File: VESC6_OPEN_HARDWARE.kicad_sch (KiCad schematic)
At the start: 22 parts, among them P1 USB_OTG, P2 CAN2, P3 SWD, P4 HALL/Encoder, P5 CAN1, P6 ADC_SWITCH

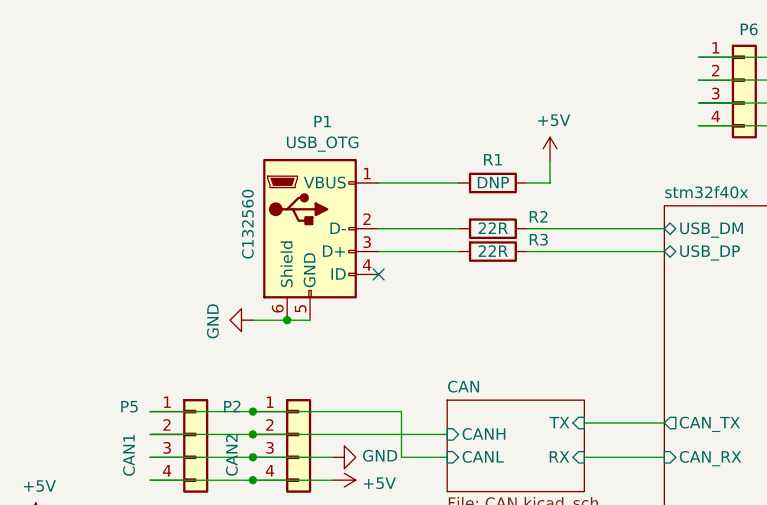
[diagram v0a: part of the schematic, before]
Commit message: added a USB-C connector and bumped the KiCAD version to 10
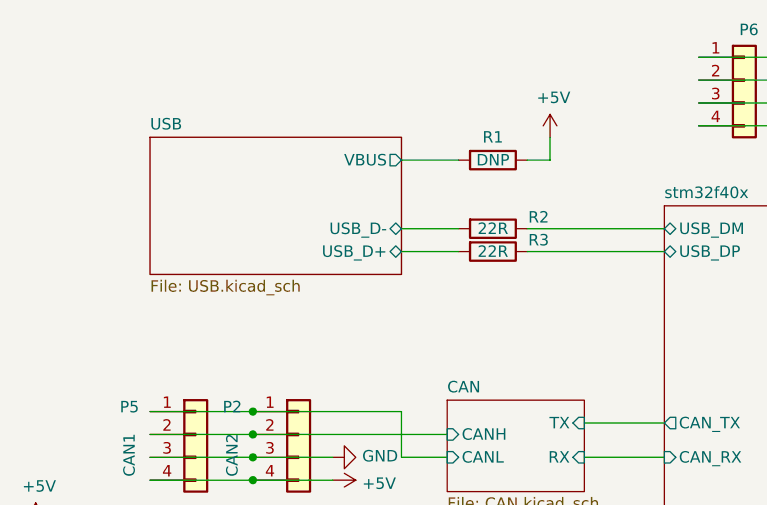
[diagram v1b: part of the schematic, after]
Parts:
- removed P1: USB_OTG, Connector_USB:USB_Micro-B_Molex_47346-0001, symbol bldc:USB_OTG
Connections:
- net USB/USB_D-: now reaches R2.2
- net USB/USB_D+: now reaches R3.2
- net USB/VBUS: now reaches R1.2
- no-connect marks 1 -> 0
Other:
- added sheet USB (USB.kicad_sch)
- moved on the sheet: R1

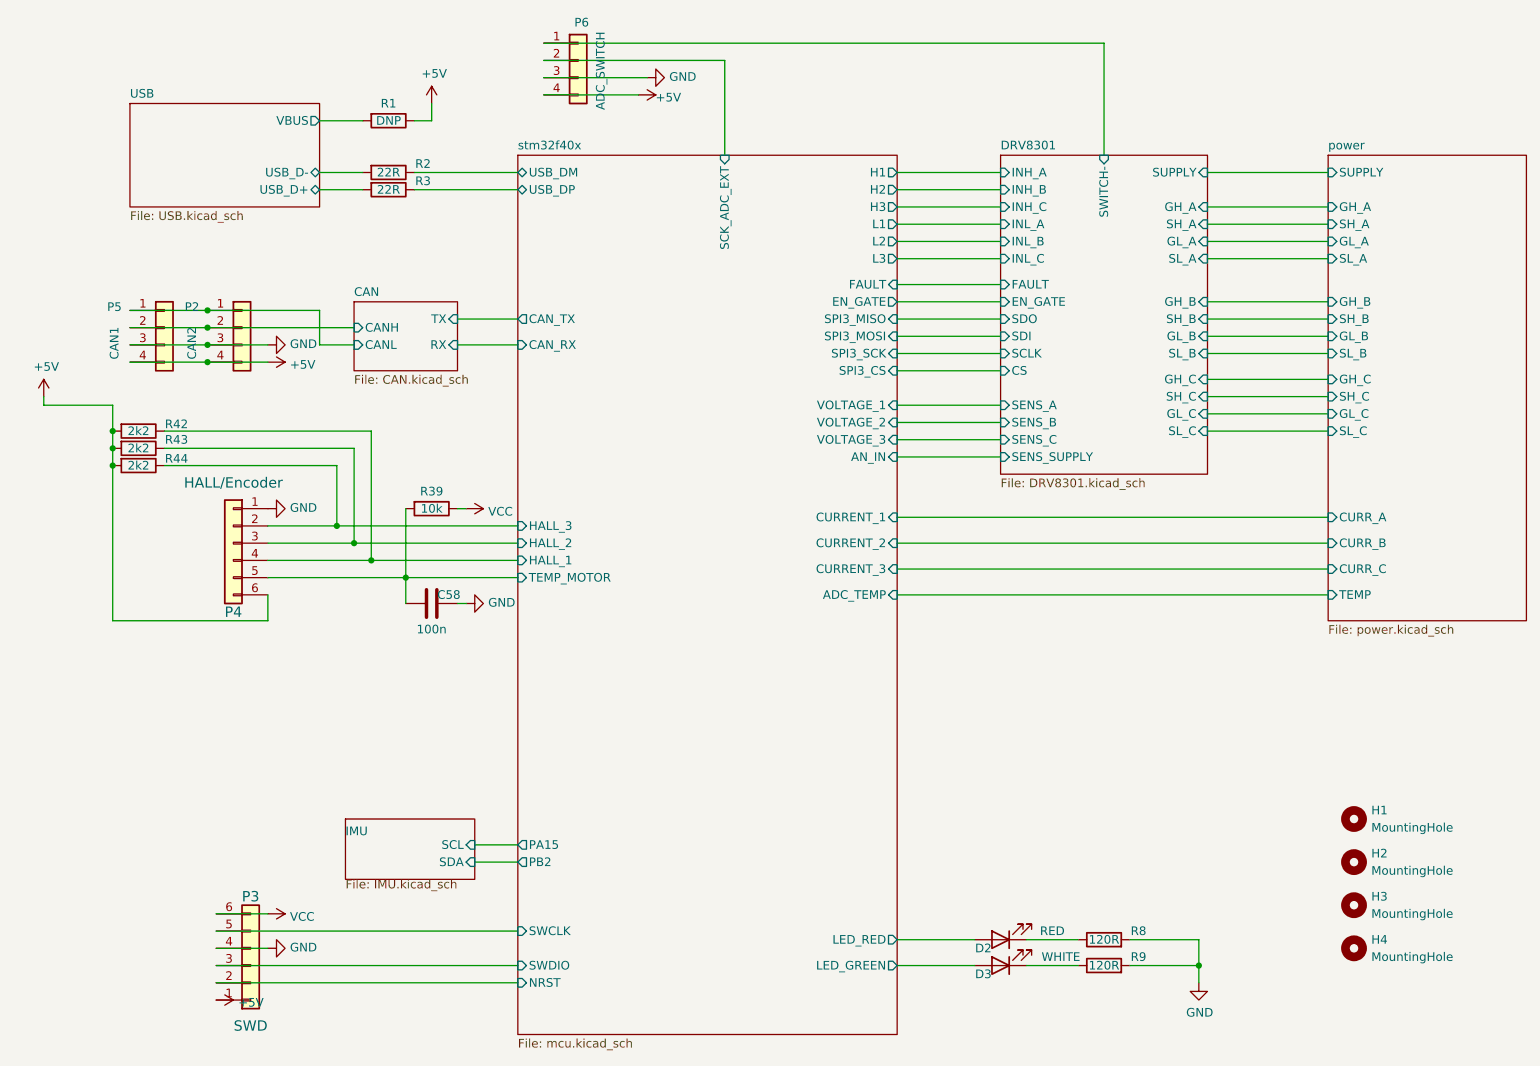
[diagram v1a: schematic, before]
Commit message: prep for chaneling. fixed the connector references, added cha to this schematic.
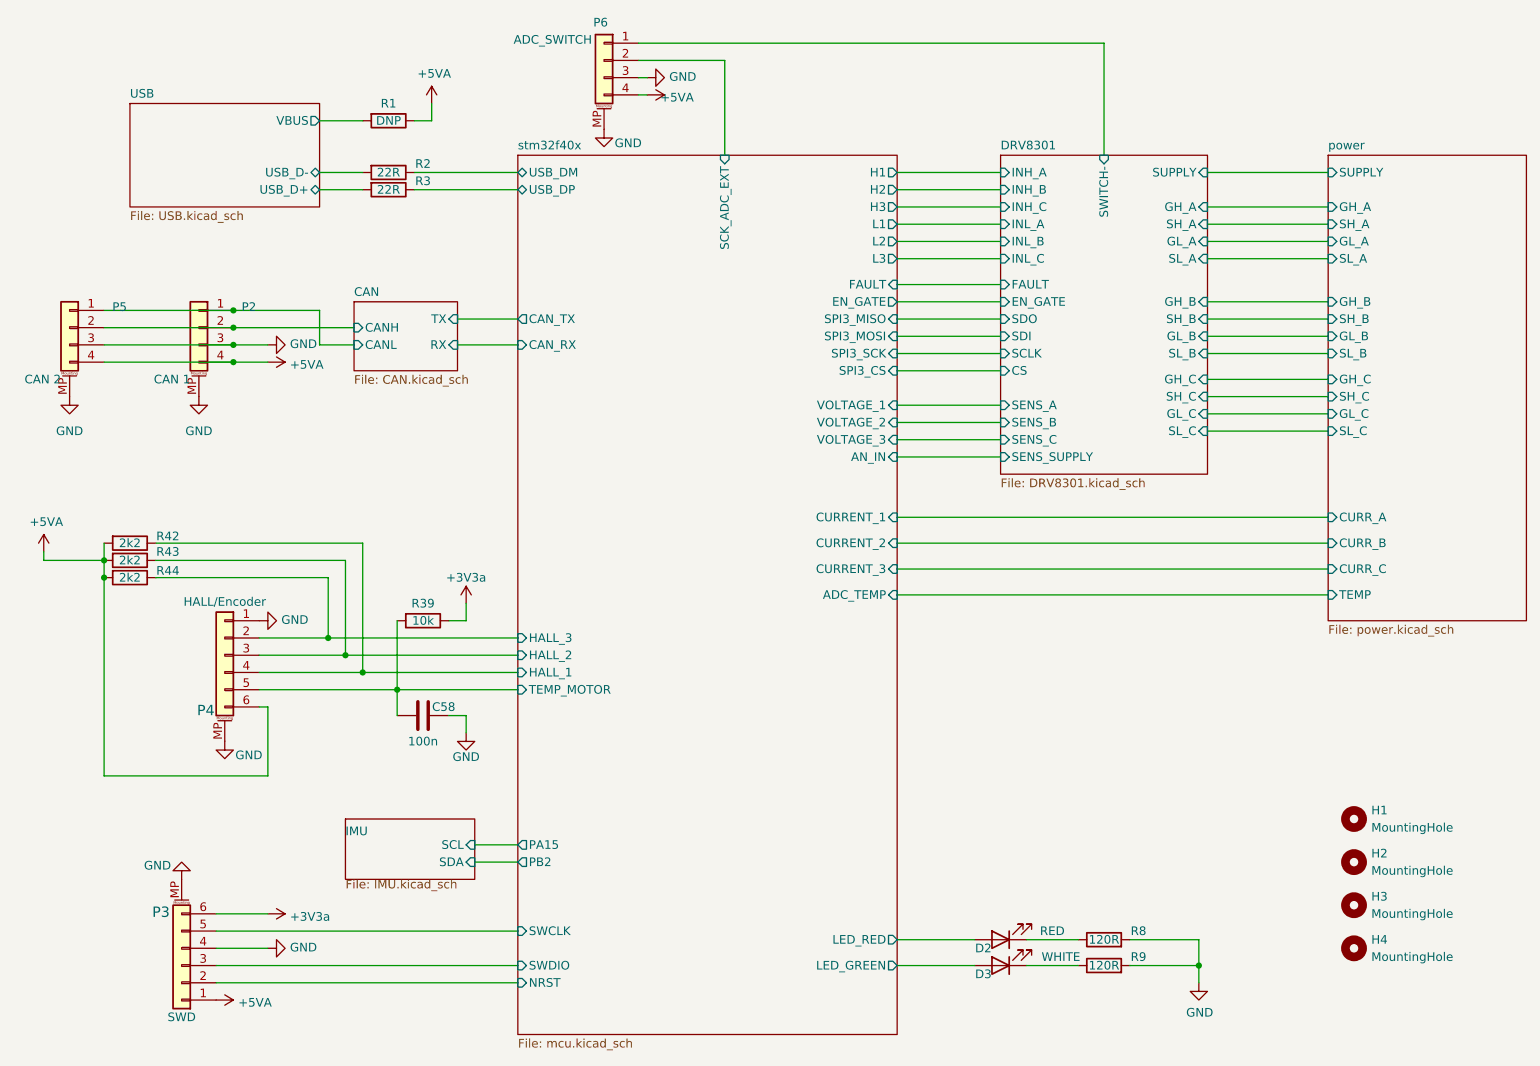
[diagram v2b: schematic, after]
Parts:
- P2: value CAN2 -> CAN 1; symbol Connector_Generic:Conn_01x04 -> Connector_Generic_MountingPin:Conn_01x04_MountingPin; Function (none) -> CAN 1
- P3: symbol Connector_Generic:Conn_01x06 -> Connector_Generic_MountingPin:Conn_01x06_MountingPin; Function (none) -> SWD
- P4: symbol Connector_Generic:Conn_01x06 -> Connector_Generic_MountingPin:Conn_01x06_MountingPin; Function (none) -> SENSE
- P5: value CAN1 -> CAN 2; symbol Connector_Generic:Conn_01x04 -> Connector_Generic_MountingPin:Conn_01x04_MountingPin; Function (none) -> CAN 2
- P6: symbol Connector_Generic:Conn_01x04 -> Connector_Generic_MountingPin:Conn_01x04_MountingPin; Function (none) -> ADC/SW
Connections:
- net GND: now also P2.MP (MountPin), P3.MP (MountPin), P4.MP (MountPin), P5.MP (MountPin), P6.MP (MountPin)
- net +5V renamed +5VA
- net VCC renamed +3V3a
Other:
- moved on the sheet: C58, R39, R42, R43, R44

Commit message: more fixes for channels
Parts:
- removed C58: 100n, Capacitor_SMD:C_0603_1608Metric, symbol Device:C
- removed D2: RED, Diode_SMD:D_0603_1608Metric, symbol Device:LED
- removed D3: WHITE, Diode_SMD:D_0603_1608Metric, symbol Device:LED
- removed P2: CAN 1, Connector_JST:JST_SH_SM04B-SRSS-TB_1x04-1MP_P1.00mm_Horizontal, symbol Connector_Generic_MountingPin:Conn_01x04_MountingPin
- removed P3: SWD, Connector_JST:JST_SH_SM06B-SRSS-TB_1x06-1MP_P1.00mm_Horizontal, symbol Connector_Generic_MountingPin:Conn_01x06_MountingPin
- removed P4: HALL/Encoder, Connector_JST:JST_SH_SM06B-SRSS-TB_1x06-1MP_P1.00mm_Horizontal, symbol Connector_Generic_MountingPin:Conn_01x06_MountingPin
- removed P5: CAN 2, Connector_JST:JST_SH_SM04B-SRSS-TB_1x04-1MP_P1.00mm_Horizontal, symbol Connector_Generic_MountingPin:Conn_01x04_MountingPin
- removed P6: ADC_SWITCH, Connector_JST:JST_SH_SM04B-SRSS-TB_1x04-1MP_P1.00mm_Horizontal, symbol Connector_Generic_MountingPin:Conn_01x04_MountingPin
- removed R1: DNP, Resistor_SMD:R_0603_1608Metric, symbol Device:R
- removed R2, R3: 22R, Resistor_SMD:R_0603_1608Metric, symbol Device:R
- removed R39: 10k, Resistor_SMD:R_0603_1608Metric, symbol Device:R
- removed R42, R43, R44: 2k2, Resistor_SMD:R_0603_1608Metric, symbol Device:R
- removed R8, R9: 120R, Resistor_SMD:R_0603_1608Metric, symbol Device:R
- renumbered H1 to H1001, H2 to H1002, H3 to H1003, H4 to H1004
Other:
- removed sheet CAN
- removed sheet DRV8301
- removed sheet IMU
- removed sheet USB
- removed sheet power
- removed sheet stm32f40x
- added sheet CHa (CHa.kicad_sch)
- added sheet CHb (CHb.kicad_sch)
- added sheet Power (power.kicad_sch)
- moved on the sheet: H1001, H1002, H1003, H1004

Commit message: it seems to work. yay
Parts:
- renumbered H1001 to H101, H1002 to H102, H1003 to H103, H1004 to H104
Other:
- moved on the sheet: H101, H102, H103, H104
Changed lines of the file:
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@@
 	(symbol
 		(lib_id "Mechanical:MountingHole")
-		(at 109.22 113.03 0)
+		(at 143.51 105.41 0)
 		(unit 1)
 		(body_style 1)
@@
 		(dnp no)
 		(fields_autoplaced yes)
-		(property "Reference" "H1001"
-			(at 111.76 111.7599 0)
+		(property "Reference" "H101"
+			(at 146.05 104.1399 0)
 			(show_name no)
 			(do_not_autoplace no)
@@
 		)
 		(property "Value" "MountingHole"
-			(at 111.76 114.2999 0)
+			(at 146.05 106.6799 0)
 			(show_name no)
 			(do_not_autoplace no)
@@
 		)
 		(property "Footprint" "CustomFootprints:MountingHole_3mm"
-			(at 109.22 113.03 0)
+			(at 143.51 105.41 0)
 			(hide yes)
 			(show_name no)
@@
 		)
 		(property "Datasheet" ""
-			(at 109.22 113.03 0)
+			(at 143.51 105.41 0)
 			(hide yes)
 			(show_name no)
@@
 		)
 		(property "Description" "Mounting Hole without connection"
-			(at 109.22 113.03 0)
-			(hide yes)
-			(show_name no)
-			(do_not_autoplace no)
-			(effects
-				(font
-					(size 1.27 1.27)
-				)
-			)
-		)
-		(instances
-			(project "VESC6_OPEN_HARDWARE"
-				(path "/8bc2c25a-a1f1-4ce8-b96a-a4f8f4c35079"
-					(reference "H1001")
+			(at 143.51 105.41 0)
+			(hide yes)
+			(show_name no)
+			(do_not_autoplace no)
+			(effects
+				(font
+					(size 1.27 1.27)
+				)
+			)
+		)
+		(instances
+			(project "VESC6_OPEN_HARDWARE"
+				(path "/8bc2c25a-a1f1-4ce8-b96a-a4f8f4c35079"
+					(reference "H101")
 					(unit 1)
 				)
@@
 	(symbol
 		(lib_id "Mechanical:MountingHole")
-		(at 109.22 119.38 0)
+		(at 143.51 111.76 0)
 		(unit 1)
 		(body_style 1)
@@
 		(dnp no)
 		(fields_autoplaced yes)
-		(property "Reference" "H1002"
-			(at 111.76 118.1099 0)
+		(property "Reference" "H102"
+			(at 146.05 110.4899 0)
 			(show_name no)
 			(do_not_autoplace no)
@@
 		)
 		(property "Value" "MountingHole"
-			(at 111.76 120.6499 0)
+			(at 146.05 113.0299 0)
 			(show_name no)
 			(do_not_autoplace no)
@@
 		)
 		(property "Footprint" "CustomFootprints:MountingHole_3mm"
-			(at 109.22 119.38 0)
+			(at 143.51 111.76 0)
 			(hide yes)
 			(show_name no)
@@
 		)
 		(property "Datasheet" ""
-			(at 109.22 119.38 0)
+			(at 143.51 111.76 0)
 			(hide yes)
 			(show_name no)
@@
 		)
 		(property "Description" "Mounting Hole without connection"
-			(at 109.22 119.38 0)
-			(hide yes)
-			(show_name no)
-			(do_not_autoplace no)
-			(effects
-				(font
-					(size 1.27 1.27)
-				)
-			)
-		)
-		(instances
-			(project "VESC6_OPEN_HARDWARE"
-				(path "/8bc2c25a-a1f1-4ce8-b96a-a4f8f4c35079"
-					(reference "H1002")
+			(at 143.51 111.76 0)
+			(hide yes)
+			(show_name no)
+			(do_not_autoplace no)
+			(effects
+				(font
+					(size 1.27 1.27)
+				)
+			)
+		)
+		(instances
+			(project "VESC6_OPEN_HARDWARE"
+				(path "/8bc2c25a-a1f1-4ce8-b96a-a4f8f4c35079"
+					(reference "H102")
 					(unit 1)
 				)
@@
 	(symbol
 		(lib_id "Mechanical:MountingHole")
-		(at 109.22 132.08 0)
+		(at 143.51 124.46 0)
 		(unit 1)
 		(body_style 1)
@@
 		(dnp no)
 		(fields_autoplaced yes)
-		(property "Reference" "H1004"
-			(at 111.76 130.8099 0)
+		(property "Reference" "H104"
+			(at 146.05 123.1899 0)
 			(show_name no)
 			(do_not_autoplace no)
@@
 		)
 		(property "Value" "MountingHole"
-			(at 111.76 133.3499 0)
+			(at 146.05 125.7299 0)
 			(show_name no)
 			(do_not_autoplace no)
@@
 		)
 		(property "Footprint" "CustomFootprints:MountingHole_3mm"
-			(at 109.22 132.08 0)
+			(at 143.51 124.46 0)
 			(hide yes)
 			(show_name no)
@@
 		)
 		(property "Datasheet" ""
-			(at 109.22 132.08 0)
+			(at 143.51 124.46 0)
 			(hide yes)
 			(show_name no)
@@
 		)
 		(property "Description" "Mounting Hole without connection"
-			(at 109.22 132.08 0)
-			(hide yes)
-			(show_name no)
-			(do_not_autoplace no)
-			(effects
-				(font
-					(size 1.27 1.27)
-				)
-			)
-		)
-		(instances
-			(project "VESC6_OPEN_HARDWARE"
-				(path "/8bc2c25a-a1f1-4ce8-b96a-a4f8f4c35079"
-					(reference "H1004")
+			(at 143.51 124.46 0)
+			(hide yes)
+			(show_name no)
+			(do_not_autoplace no)
+			(effects
+				(font
+					(size 1.27 1.27)
+				)
+			)
+		)
+		(instances
+			(project "VESC6_OPEN_HARDWARE"
+				(path "/8bc2c25a-a1f1-4ce8-b96a-a4f8f4c35079"
+					(reference "H104")
 					(unit 1)
 				)
@@
 	(symbol
 		(lib_id "Mechanical:MountingHole")
-		(at 109.22 125.73 0)
+		(at 143.51 118.11 0)
 		(unit 1)
 		(body_style 1)
@@
 		(dnp no)
 		(fields_autoplaced yes)
-		(property "Reference" "H1003"
-			(at 111.76 124.4599 0)
+		(property "Reference" "H103"
+			(at 146.05 116.8399 0)
 			(show_name no)
 			(do_not_autoplace no)
@@
 		)
 		(property "Value" "MountingHole"
-			(at 111.76 126.9999 0)
+			(at 146.05 119.3799 0)
 			(show_name no)
 			(do_not_autoplace no)
@@
 		)
 		(property "Footprint" "CustomFootprints:MountingHole_3mm"
-			(at 109.22 125.73 0)
+			(at 143.51 118.11 0)
 			(hide yes)
 			(show_name no)
@@
 		)
 		(property "Datasheet" ""
-			(at 109.22 125.73 0)
+			(at 143.51 118.11 0)
 			(hide yes)
 			(show_name no)
@@
 		)
 		(property "Description" "Mounting Hole without connection"
-			(at 109.22 125.73 0)
-			(hide yes)
-			(show_name no)
-			(do_not_autoplace no)
-			(effects
-				(font
-					(size 1.27 1.27)
-				)
-			)
-		)
-		(instances
-			(project "VESC6_OPEN_HARDWARE"
-				(path "/8bc2c25a-a1f1-4ce8-b96a-a4f8f4c35079"
-					(reference "H1003")
+			(at 143.51 118.11 0)
+			(hide yes)
+			(show_name no)
+			(do_not_autoplace no)
+			(effects
+				(font
+					(size 1.27 1.27)
+				)
+			)
+		)
+		(instances
+			(project "VESC6_OPEN_HARDWARE"
+				(path "/8bc2c25a-a1f1-4ce8-b96a-a4f8f4c35079"
+					(reference "H103")
 					(unit 1)
 				)
@@
 	)
 	(sheet
-		(at 118.11 55.88)
-		(size 38.1 25.4)
+		(at 82.55 41.91)
+		(size 53.34 34.29)
 		(exclude_from_sim no)
 		(in_bom yes)
@@
 		)
 		(property "Sheetname" "CHa"
-			(at 118.11 55.1684 0)
+			(at 82.55 41.1984 0)
 			(show_name no)
 			(do_not_autoplace no)
@@
 		)
 		(property "Sheetfile" "CHa.kicad_sch"
-			(at 118.11 81.8646 0)
+			(at 82.55 76.7846 0)
 			(show_name no)
 			(do_not_autoplace no)
@@
 			(project "VESC6_OPEN_HARDWARE"
 				(path "/8bc2c25a-a1f1-4ce8-b96a-a4f8f4c35079"
-					(page "9")
+					(page "3")
 				)
 			)
@@
 	)
 	(sheet
-		(at 76.2 55.88)
+		(at 109.22 101.6)
 		(size 29.21 25.4)
 		(exclude_from_sim no)
@@
 		)
 		(property "Sheetname" "Power"
-			(at 76.2 55.1684 0)
+			(at 109.22 100.8884 0)
 			(show_name no)
 			(do_not_autoplace no)
@@
 		)
 		(property "Sheetfile" "power.kicad_sch"
-			(at 76.2 81.8646 0)
+			(at 109.22 127.5846 0)
 			(show_name no)
 			(do_not_autoplace no)
@@
 			(project "VESC6_OPEN_HARDWARE"
 				(path "/8bc2c25a-a1f1-4ce8-b96a-a4f8f4c35079"
-					(page "8")
+					(page "2")
 				)
 			)
@@
 	)
 	(sheet
-		(at 161.29 55.88)
-		(size 40.64 25.4)
+		(at 143.51 41.91)
+		(size 53.34 34.29)
 		(exclude_from_sim no)
 		(in_bom yes)
@@
 		)
 		(property "Sheetname" "CHb"
-			(at 161.29 55.1684 0)
+			(at 143.51 41.1984 0)
 			(show_name no)
 			(do_not_autoplace no)
@@
 		)
 		(property "Sheetfile" "CHb.kicad_sch"
-			(at 161.29 81.8646 0)
+			(at 143.51 76.7846 0)
 			(show_name no)
 			(do_not_autoplace no)
@@
 			(project "VESC6_OPEN_HARDWARE"
 				(path "/8bc2c25a-a1f1-4ce8-b96a-a4f8f4c35079"
-					(page "10")
-				)
-			)
+					(page "4")
+				)
+			)

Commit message: small improvements.
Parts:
- added H105: MountingHole, CustomFootprints:MountingHole_3mm, symbol Mechanical:MountingHole
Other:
- sheet CHa ports: added CANH, CANL; removed none
- sheet CHb ports: added CANH, CANL; removed none
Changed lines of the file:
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@@
 		(comment 1 "Drawn By: CG")
+	)
+	(wire
+		(pts
+			(xy 135.89 58.42) (xy 143.51 58.42)
+		)
+		(stroke
+			(width 0)
+			(type default)
+		)
+	)
+	(wire
+		(pts
+			(xy 135.89 54.61) (xy 143.51 54.61)
+		)
+		(stroke
+			(width 0)
+			(type default)
+		)
 	)
 	(symbol
@@
 	(symbol
 		(lib_id "Mechanical:MountingHole")
+		(at 143.51 130.81 0)
+		(unit 1)
+		(body_style 1)
+		(exclude_from_sim no)
+		(in_bom no)
+		(on_board yes)
+		(in_pos_files yes)
+		(dnp no)
+		(fields_autoplaced yes)
+		(property "Reference" "H105"
+			(at 146.05 129.5399 0)
+			(show_name no)
+			(do_not_autoplace no)
+			(effects
+				(font
+					(size 1.27 1.27)
+				)
+				(justify left)
+			)
+		)
+		(property "Value" "MountingHole"
+			(at 146.05 132.0799 0)
+			(show_name no)
+			(do_not_autoplace no)
+			(effects
+				(font
+					(size 1.27 1.27)
+				)
+				(justify left)
+			)
+		)
+		(property "Footprint" "CustomFootprints:MountingHole_3mm"
+			(at 143.51 130.81 0)
+			(hide yes)
+			(show_name no)
+			(do_not_autoplace no)
+			(effects
+				(font
+					(size 1.27 1.27)
+				)
+			)
+		)
+		(property "Datasheet" ""
+			(at 143.51 130.81 0)
+			(hide yes)
+			(show_name no)
+			(do_not_autoplace no)
+			(effects
+				(font
+					(size 1.27 1.27)
+				)
+			)
+		)
+		(property "Description" "Mounting Hole without connection"
+			(at 143.51 130.81 0)
+			(hide yes)
+			(show_name no)
+			(do_not_autoplace no)
+			(effects
+				(font
+					(size 1.27 1.27)
+				)
+			)
+		)
+		(instances
+			(project "VESC6_OPEN_HARDWARE"
+				(path "/8bc2c25a-a1f1-4ce8-b96a-a4f8f4c35079"
+					(reference "H105")
+					(unit 1)
+				)
+			)
+		)
+	)
+	(symbol
+		(lib_id "Mechanical:MountingHole")
 		(at 143.51 118.11 0)
 		(unit 1)
@@
 			)
 		)
+		(pin "CANH" bidirectional
+			(at 135.89 54.61 0)
+			(effects
+				(font
+					(size 1.27 1.27)
+				)
+				(justify right)
+			)
+		)
+		(pin "CANL" bidirectional
+			(at 135.89 58.42 0)
+			(effects
+				(font
+					(size 1.27 1.27)
+				)
+				(justify right)
+			)
+		)
 		(instances
 			(project "VESC6_OPEN_HARDWARE"
@@
 			)
 		)
+		(pin "CANH" bidirectional
+			(at 143.51 54.61 180)
+			(effects
+				(font
+					(size 1.27 1.27)
+				)
+				(justify left)
+			)
+		)
+		(pin "CANL" bidirectional
+			(at 143.51 58.42 180)
+			(effects
+				(font
+					(size 1.27 1.27)
+				)
+				(justify left)
+			)
+		)

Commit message: more tweaks
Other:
- company: (none) -> craigg96, Tomáš Kuchta
- title: (none) -> 2ch VESC based on VESC6
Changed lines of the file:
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@@
 	(paper "A4")
 	(title_block
+		(title "2ch VESC based on VESC6")
 		(date "2025-03-23")
-		(rev "A")
-		(comment 1 "Drawn By: CG")
+		(rev "B")
+		(company "craigg96, Tomáš Kuchta")
 	)
 	(wire
